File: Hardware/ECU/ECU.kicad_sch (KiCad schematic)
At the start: 4 parts, among them U1 Teensy4.1

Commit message: new file:   Hardware/ECU/ECU-backups/ECU-2024-11-06_180755.zip 	new file:   Hardware/ECU/ECU-backups/ECU-2024-11-06_185548.zip 	new file:   Hardware/ECU/ECU-backups/ECU-2024-11-06_190414.zip 	new file:   Hardware/ECU/ECU-backups/ECU-2024-11-06_191218.zip 	new file:   Hardware/ECU/ECU-backups/ECU-2024-11-06_192808.zip 	modified:   Hardware/ECU/ECU.kicad_pro 	modified:   Hardware/ECU/ECU.kicad_sch 	deleted:    Hardware/ECU/~ECU.kicad_sch.lck
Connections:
- net MC33814-CS: now also U1.4 (2_OUT2)
- net MCU-A0: now also U1.40 (18_A4_SDA)
- net MCU-A1: now also U1.41 (19_A5_SCL)
- net MCU-A14: now also U1.31 (39_MISO1_OUT1A)
- net MCU-A15: now also U1.28 (36_CS)
- net MCU-A16: now also U1.29 (37_CS)
- net MCU-A17: now also U1.32 (40_A16)
- net MCU-A18: now also U1.33 (41_A17)
- net MCU-A19: now also U1.36 (14_A0_TX3_SPDIF_OUT)
- net MCU-A20: now also U1.37 (15_A1_RX3_SPDIF_IN)
- net MCU-A21: now also U1.38 (16_A2_RX4_SCL1)
- net MCU-A22: now also U1.39 (17_A3_TX4_SDA1)
- net MCU-A4: now also U1.42 (20_A6_TX5_LRCLK1)
- net MCU-A5: now also U1.43 (21_A7_RX5_BCLK1)
- net MCU-A8: now also U1.44 (22_A8_CTX1)
- net MCU-A9: now also U1.45 (23_A9_CRX1_MCLK1)
- net MCU-D0: now also U1.2 (0_RX1_CRX2_CS1)
- net MCU-D1: now also U1.3 (1_TX1_CTX2_MISO1)
- net MCU-D10: now also U1.12 (10_CS_MQSR)
- net MCU-D24: now also U1.16 (24_A10_TX6_SCL2)
- net MCU-D25: now also U1.17 (25_A11_RX6_SDA2)
- net MCU-D26: now also U1.18 (26_A12_MOSI1)
- net MCU-D27: now also U1.19 (27_A13_SCK1)
- net MCU-D28: now also U1.20 (28_RX7)
- net MCU-D29: now also U1.21 (29_TX7)
- net MCU-D3: now also U1.5 (3_LRCLK2)
- net MCU-D30: now also U1.22 (30_CRX3)
- net MCU-D31: now also U1.23 (31_CTX3)
- net MCU-D32: now also U1.24 (32_OUT1B)
- net MCU-D4: now also U1.6 (4_BCLK2)
- net MCU-D5: now also U1.7 (5_IN2)
- net MCU-D6: now also U1.8 (6_OUT1D)
- net MCU-D7: now also U1.9 (7_RX2_OUT1A)
- net MCU-D8: now also U1.10 (8_TX2_IN1)
- net MCU-D9: now also U1.11 (9_OUT1C)
- net MISO: now also U1.14 (12_MISO_MQSL)
- net MOSI: now also U1.13 (11_MOSI_CTX1)
- net PROG: now also U1.53 (PROGRAM)
- net RESET: now also U1.54 (ON_OFF)
- net SCLK: now also U1.35 (13_SCK_LED)
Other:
- note added: "NC"

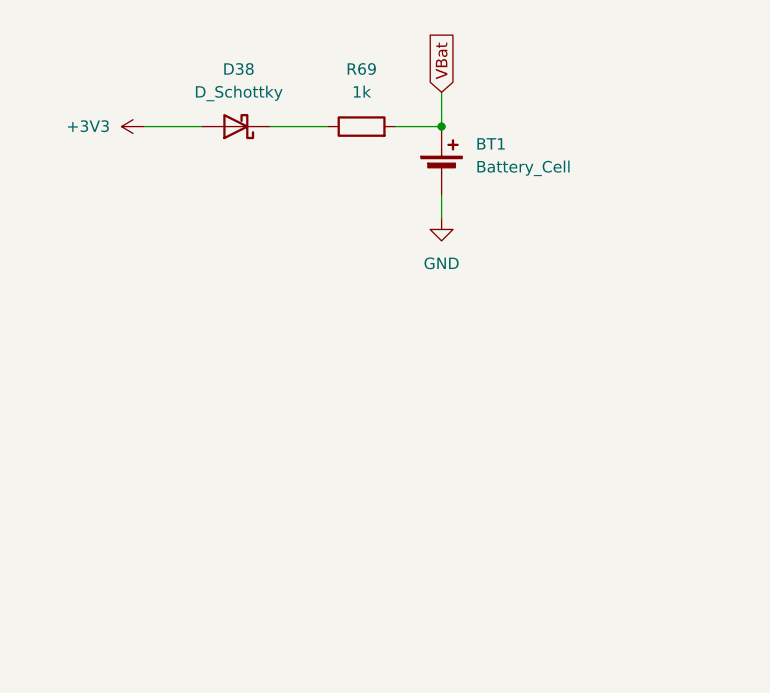
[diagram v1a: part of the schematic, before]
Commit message: modified:   .gitmodules 	modified:   Hardware/ECU/Comms.kicad_sch 	modified:   Hardware/ECU/ECU.kicad_pcb 	modified:   Hardware/ECU/ECU.kicad_pro 	modified:   Hardware/ECU/ECU.kicad_sch 	modified:   Hardware/ECU/Inputs.kicad_sch 	modified:   Hardware/ECU/Outputs.kicad_sch 	modified:   Hardware/ECU/fp-info-cache 	modified:   Hardware/ECU/fp-lib-table 	deleted:    docs/ECU info.url 	modified:   tune/Hayabusa-R1/CurrentTune.msq 	modified:   tune/Hayabusa-R1/projectCfg/project.properties 	modified:   tune/Hayabusa-R1/projectCfg/project.properties.bkup 	Hardware/ECU/ECU-backups/ECU-2024-11-07_084642.zip 	Hardware/ECU/ECU-backups/ECU-2024-11-07_091524.zip 	Hardware/ECU/ECU-backups/ECU-2024-11-07_094217.zip 	Hardware/ECU/ECU-backups/ECU-2024-11-07_120300.zip 	Hardware/ECU/ECU-backups/ECU-2024-11-08_085235.zip 	Hardware/ECU/ECU-backups/ECU-2024-11-08_091401.zip 	Hardware/ECU/ECU-backups/ECU-2024-11-08_103901.zip 	Hardware/ECU/docs/ 	Hardware/ECU/lib/2999/ 	Hardware/ECU/lib/IC_Automotive/IC_Automotive.pretty/BAT_2999.kicad_mod 	Hardware/ECU/lib/IC_Automotive/IC_Automotive.pretty/ZXMS6006DT8TA.kicad_mod 	Hardware/ECU/lib/ZXMS6006DT8TA/ 	Hardware/ECU/lib/teensy_library/ 	Hardware/ECU/output.pdf 	Hardware/ECU/report.txt 	docs/Speeduino_manual.pdf 	docs/Speeduino_manual.pdf:Zone.Identifier 	tune/Hayabusa-R1/dashboard/lambdaTable1Map.dash 	tune/Hayabusa-R1/dashboard/stagingMap.dash 	tune/TunerStudioAppDebug.txt
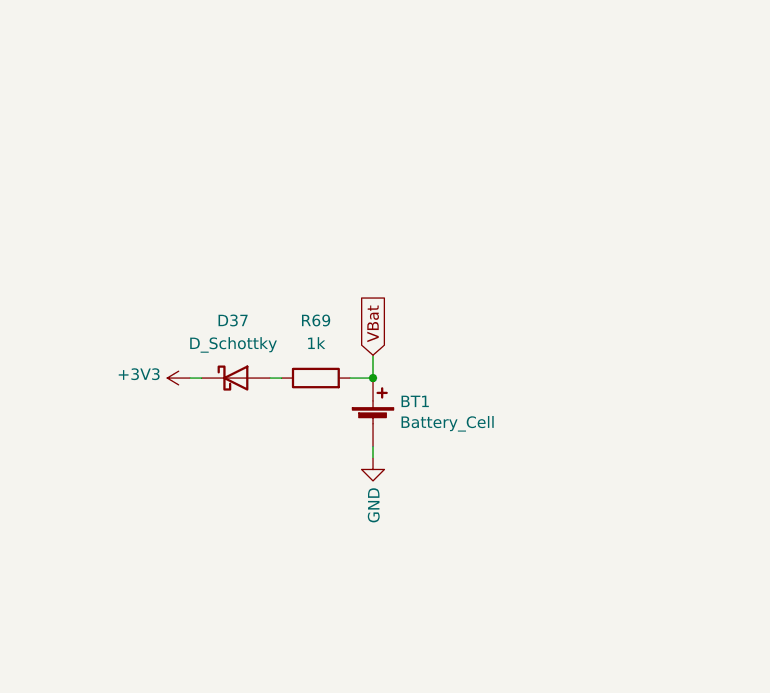
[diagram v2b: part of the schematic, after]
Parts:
- removed D38: D_Schottky, symbol Device:D_Schottky
- added D37: D_Schottky, Diode_SMD:D_PowerDI-123, symbol Device:D_Schottky
- BT1: footprint (none) -> 2999:BAT_2999; Digikey Part Number (none) -> 36-2999-ND; Manufacturer_Name (none) -> Keystone; Manufacturer_Part_Number (none) -> 2999; URL (none) -> https://www.digikey.com.au/product-detail/en/keystone-elect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
- R69: footprint (none) -> Resistor_SMD:R_0805_2012Metric; Digikey Part Number (none) -> 311-1.00KCRCT-ND; Manufacturer_Name (none) -> Yageo; Manufacturer_Part_Number (none) -> RC0805FR-071KL; URL (none) -> https://www.digikey.com/product-detail/en/yageo/RC0805FR-07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
- U1: footprint (none) -> kicad:Teensy41
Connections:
- net +3V3: now also D37.1 (K)
- net at R69.1: now also D37.2 (A)

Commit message: modified:   Hardware/ECU/Conntectors.kicad_sch 	deleted:    Hardware/ECU/ECU-backups/ECU-2024-10-31_195121.zip 	deleted:    Hardware/ECU/ECU-backups/ECU-2024-10-31_200337.zip 	deleted:    Hardware/ECU/ECU-backups/ECU-2024-10-31_204750.zip 	deleted:    Hardware/ECU/ECU-backups/ECU-2024-10-31_205306.zip 	deleted:    Hardware/ECU/ECU-backups/ECU-2024-10-31_224509.zip 	deleted:    Hardware/ECU/ECU-backups/ECU-2024-11-01_010106.zip 	deleted:    Hardware/ECU/ECU-backups/ECU-2024-11-05_092146.zip 	modified:   Hardware/ECU/ECU.kicad_sch 	deleted:    Hardware/ECU/docs/0900766b80fa0058.pdf:Zone.Identifier 	deleted:    Hardware/ECU/docs/155849888-9-6437288-3.zip:Zone.Identifier 	deleted:    Hardware/ECU/docs/155850325-21-6437288-3.zip:Zone.Identifier 	deleted:    Hardware/ECU/docs/ECM-pinout.pdf 	deleted:    docs/08ecubusapinout.jpg 	deleted:    docs/suzuki-gsx-1300-r-hayabusa-1999-2003-service-manual.pdf:Zone.Identifier 	modified:   speeduino 	Hardware/ECU/ECU-backups/ECU-2024-12-18_220608.zip 	Hardware/ECU/ECU-backups/ECU-2024-12-30_215431.zip 	Hardware/ECU/ECU-backups/ECU-2024-12-31_001349.zip 	Hardware/ECU/ECU-backups/ECU-2025-01-02_140333.zip 	Hardware/ECU/ECU-backups/ECU-2025-01-02_142840.zip 	Hardware/ECU/ECU-backups/ECU-2025-01-02_150227.zip 	Hardware/ECU/ECU-backups/ECU-2025-01-03_004705.zip 	Hardware/ECU/ECU-backups/ECU-2025-01-03_005407.zip 	Hardware/ECU/ECU-backups/ECU-2025-01-03_013204.zip 	Hardware/ECU/ECU-backups/ECU-2025-01-03_020554.zip 	Hardware/ECU/docs/Pinout.ods
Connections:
- net GND: no longer U1.58 (GND)
- net USB 5V: now reaches U1.55 (5V)
- net USB D-: now reaches U1.56 (D-)
- net USB D+: now reaches U1.57 (D+)
- new net USB GND: U1.58 (GND)
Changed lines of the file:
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@@
+	(wire
+		(pts
+			(xy 134.62 120.65) (xy 139.7 120.65)
+		)
+		(stroke
+			(width 0)
+			(type default)
+		)
+	)
 	(wire
 		(pts
@@
 	(wire
 		(pts
+			(xy 134.62 115.57) (xy 139.7 115.57)
+		)
+		(stroke
+			(width 0)
+			(type default)
+		)
+	)
+	(wire
+		(pts
 			(xy 34.29 54.61) (xy 35.56 54.61)
 		)
@@
 	(wire
 		(pts
-			(xy 135.89 120.65) (xy 139.7 120.65)
+			(xy 134.62 118.11) (xy 139.7 118.11)
 		)
 		(stroke
@@
 		(pts
 			(xy 195.58 60.96) (xy 199.39 60.96)
+		)
+		(stroke
+			(width 0)
+			(type default)
+		)
+	)
+	(wire
+		(pts
+			(xy 134.62 113.03) (xy 139.7 113.03)
 		)
 		(stroke
@@
 		)
 	)
+	(global_label "USB 5V"
+		(shape input)
+		(at 134.62 113.03 180)
+		(fields_autoplaced yes)
+		(effects
+			(font
+				(size 1.27 1.27)
+			)
+			(justify right)
+		)
+		(property "Intersheetrefs" "${INTERSHEET_REFS}"
+			(at 124.5591 113.03 0)
+			(effects
+				(font
+					(size 1.27 1.27)
+				)
+				(justify right)
+				(hide yes)
+			)
+		)
+	)
 	(global_label "MCU-A0"
 		(shape input)
@@
 		)
 	)
+	(global_label "USB D+"
+		(shape input)
+		(at 134.62 118.11 180)
+		(fields_autoplaced yes)
+		(effects
+			(font
+				(size 1.27 1.27)
+			)
+			(justify right)
+		)
+		(property "Intersheetrefs" "${INTERSHEET_REFS}"
+			(at 124.0148 118.11 0)
+			(effects
+				(font
+					(size 1.27 1.27)
+				)
+				(justify right)
+				(hide yes)
+			)
+		)
+	)
 	(global_label "MCU-D25"
 		(shape input)
@@
 		(property "Intersheetrefs" "${INTERSHEET_REFS}"
 			(at 210.806 53.34 0)
+			(effects
+				(font
+					(size 1.27 1.27)
+				)
+				(justify right)
+				(hide yes)
+			)
+		)
+	)
+	(global_label "USB GND"
+		(shape input)
+		(at 134.62 120.65 180)
+		(fields_autoplaced yes)
+		(effects
+			(font
+				(size 1.27 1.27)
+			)
+			(justify right)
+		)
+		(property "Intersheetrefs" "${INTERSHEET_REFS}"
+			(at 122.9867 120.65 0)
+			(effects
+				(font
+					(size 1.27 1.27)
+				)
+				(justify right)
+				(hide yes)
+			)
+		)
+	)
+	(global_label "USB D-"
+		(shape input)
+		(at 134.62 115.57 180)
+		(fields_autoplaced yes)
+		(effects
+			(font
+				(size 1.27 1.27)
+			)
+			(justify right)
+		)
+		(property "Intersheetrefs" "${INTERSHEET_REFS}"
+			(at 124.0148 115.57 0)
 			(effects
 				(font
@@
 	(symbol
 		(lib_id "power:GND")
-		(at 135.89 120.65 270)
+		(at 236.22 116.84 270)
 		(unit 1)
 		(exclude_from_sim no)
@@
 		(dnp no)
 		(property "Reference" "#PWR0124"
-			(at 129.54 120.65 0)
+			(at 229.87 116.84 0)
 			(effects
 				(font
@@
 		)
 		(property "Value" "GND"
-			(at 132.6388 120.777 90)
+			(at 232.9688 116.967 90)
 			(effects
 				(font
@@
 		)
 		(property "Footprint" ""
-			(at 135.89 120.65 0)
+			(at 236.22 116.84 0)
 			(effects
 				(font
@@
 		)
 		(property "Datasheet" ""
-			(at 135.89 120.65 0)
+			(at 236.22 116.84 0)
 			(effects
 				(font
@@
 		)
 		(property "Description" ""
-			(at 135.89 120.65 0)
-			(effects
-				(font
+			(at 236.22 116.84 0)
+			(effects
+				(font

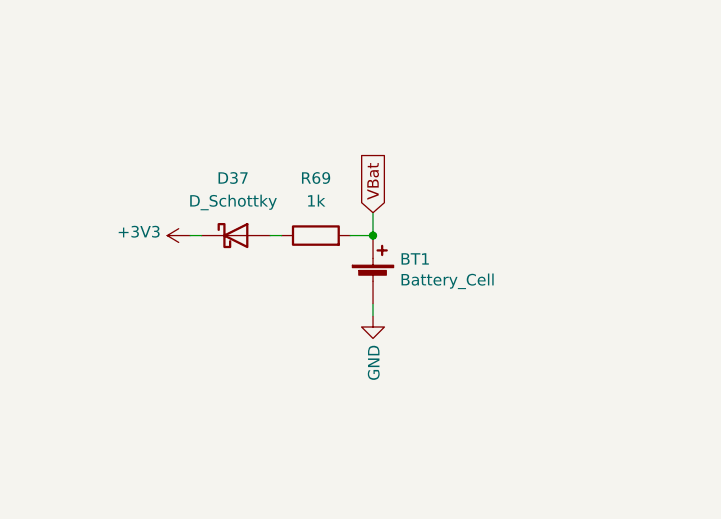
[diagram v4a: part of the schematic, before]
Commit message: PCB V0.1
Erste Iteration der PCB vernetzt
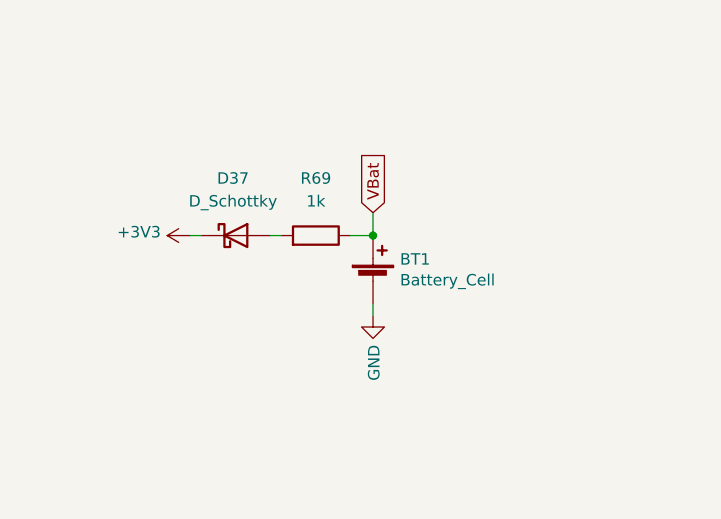
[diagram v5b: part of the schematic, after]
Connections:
- net VBat: now also R69.1; no longer R69.2
- net at D37.2 (A): now also R69.2; no longer R69.1
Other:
- moved on the sheet: R69
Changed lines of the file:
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@@
 	(symbol
 		(lib_id "Device:R")
-		(at 48.26 54.61 90)
+		(at 48.26 54.61 270)
+		(mirror x)
 		(unit 1)
 		(exclude_from_sim no)
@@
 		(on_board yes)
 		(dnp no)
-		(fields_autoplaced yes)
 		(property "Reference" "R69"
 			(at 48.26 48.26 90)

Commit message: renamed:    Hardware/ECU/ECU-backups/ECU-2025-05-27_141528.zip -> Hardware/ECU/ECU-backups/ECU-2025-05-27_234640.zip 	renamed:    Hardware/ECU/ECU-backups/ECU-2025-05-27_154948.zip -> Hardware/ECU/ECU-backups/ECU-2025-05-27_235240.zip 	modified:   Hardware/ECU/ECU.kicad_pcb 	modified:   Hardware/ECU/ECU.kicad_prl 	modified:   Hardware/ECU/ECU.kicad_sch
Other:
- note removed: "NC"

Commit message: deleted:    Hardware/ECU/ECU-backups/ECU-2025-05-27_235240.zip 	deleted:    Hardware/ECU/ECU-backups/ECU-2025-05-28_135321.zip 	deleted:    Hardware/ECU/ECU-backups/ECU-2025-05-28_140049.zip 	deleted:    Hardware/ECU/ECU-backups/ECU-2025-05-28_141416.zip 	deleted:    Hardware/ECU/ECU-backups/ECU-2025-05-28_154718.zip 	deleted:    Hardware/ECU/ECU-backups/ECU-2025-06-18_111329.zip 	new file:   Hardware/ECU/ECU-backups/ECU-2025-08-26_154141.zip 	new file:   Hardware/ECU/ECU-backups/ECU-2025-08-29_143817.zip 	new file:   Hardware/ECU/ECU-backups/ECU-2025-09-19_081818.zip 	new file:   Hardware/ECU/ECU-backups/ECU-2026-01-19_151411.zip 	new file:   Hardware/ECU/ECU-backups/ECU-2026-01-19_152057.zip 	new file:   Hardware/ECU/ECU-backups/ECU-2026-01-19_154705.zip 	modified:   Hardware/ECU/ECU.kicad_pcb 	modified:   Hardware/ECU/ECU.kicad_prl 	modified:   Hardware/ECU/ECU.kicad_sch 	modified:   Hardware/ECU/Inputs.kicad_sch 	modified:   Hardware/ECU/Inputs2.kicad_sch 	renamed:    Hardware/ECU/output/PCB.pdf -> Hardware/ECU/output/PCB-R9.3.pdf 	renamed:    Hardware/ECU/output/Schematics.pdf -> Hardware/ECU/output/Schematics-R0.3.pdf 	new file:   Hardware/ECU/output/Schematics-R1.pdf 	deleted:    Hardware/ECU/output/cut files/ECU-B_Cu.jpg 	modified:   speeduino (modified content)
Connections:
- net MCU-A18 is gone; now on net MCU-A17: U1.33 (41_A17)
- net MCU-A19 is gone; now on net MCU-A0: U1.36 (14_A0_TX3_SPDIF_OUT)
- net MCU-A20 is gone; now on net MCU-A1: U1.37 (15_A1_RX3_SPDIF_IN)
- net MCU-A0: no longer U1.40 (18_A4_SDA)
- net MCU-A1: no longer U1.41 (19_A5_SCL)
- net MCU-A14: now also U1.30 (38_CS1_IN1); no longer U1.31 (39_MISO1_OUT1A)
- net MCU-A15: now also U1.31 (39_MISO1_OUT1A); no longer U1.28 (36_CS)
- net MCU-A16: now also U1.32 (40_A16); no longer U1.29 (37_CS)
- net MCU-A17: no longer U1.32 (40_A16)
- net MCU-A4: now also U1.40 (18_A4_SDA); no longer U1.42 (20_A6_TX5_LRCLK1)
- net MCU-A5: now also U1.41 (19_A5_SCL); no longer U1.43 (21_A7_RX5_BCLK1)
- net MCU-A21 renamed MCU-A2
- net MCU-A22 renamed MCU-A3
- net MCU-A8 renamed MCU-D22
- net MCU-A9 renamed MCU-D23
- new net MCU-D18: U1.42 (20_A6_TX5_LRCLK1)
- new net MCU-D19: U1.43 (21_A7_RX5_BCLK1)
- new net MCU-D36: U1.28 (36_CS)
